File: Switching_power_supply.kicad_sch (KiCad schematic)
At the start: 20 parts, among them J10 Conn_01x02, J11 Conn_01x02, J12 Conn_01x02, J8 Conn_01x03_Pin, J9 Conn_01x02, U4 AMS1117, U5 LM2596HVS-ADJRG

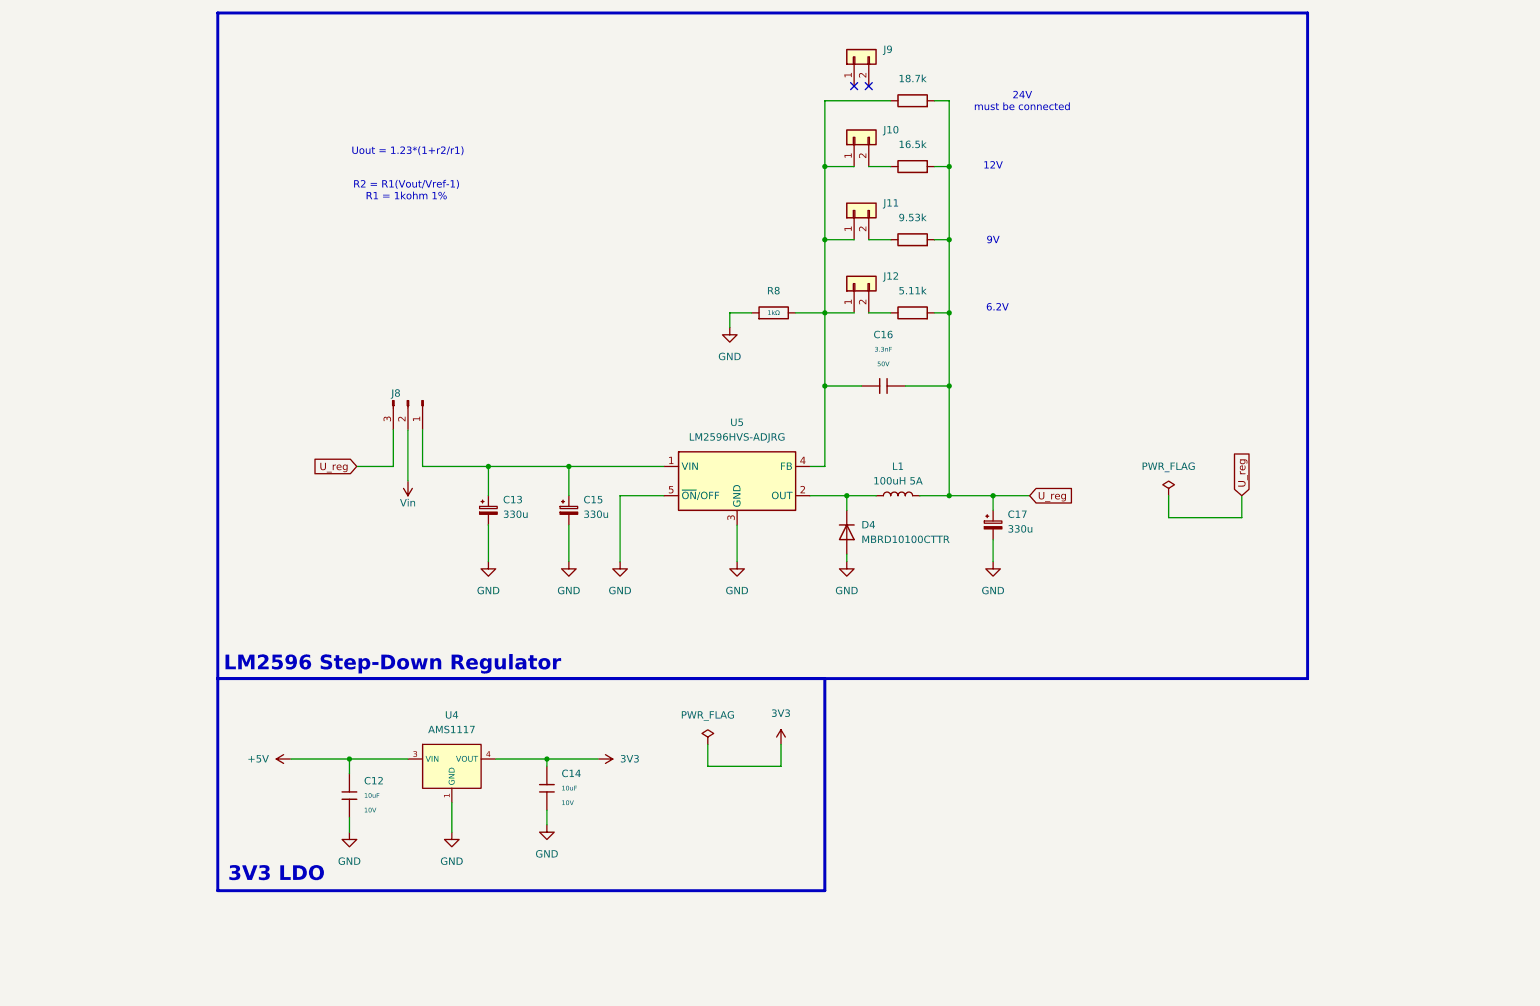
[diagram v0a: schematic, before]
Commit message: Added mechanical standard and updated readme
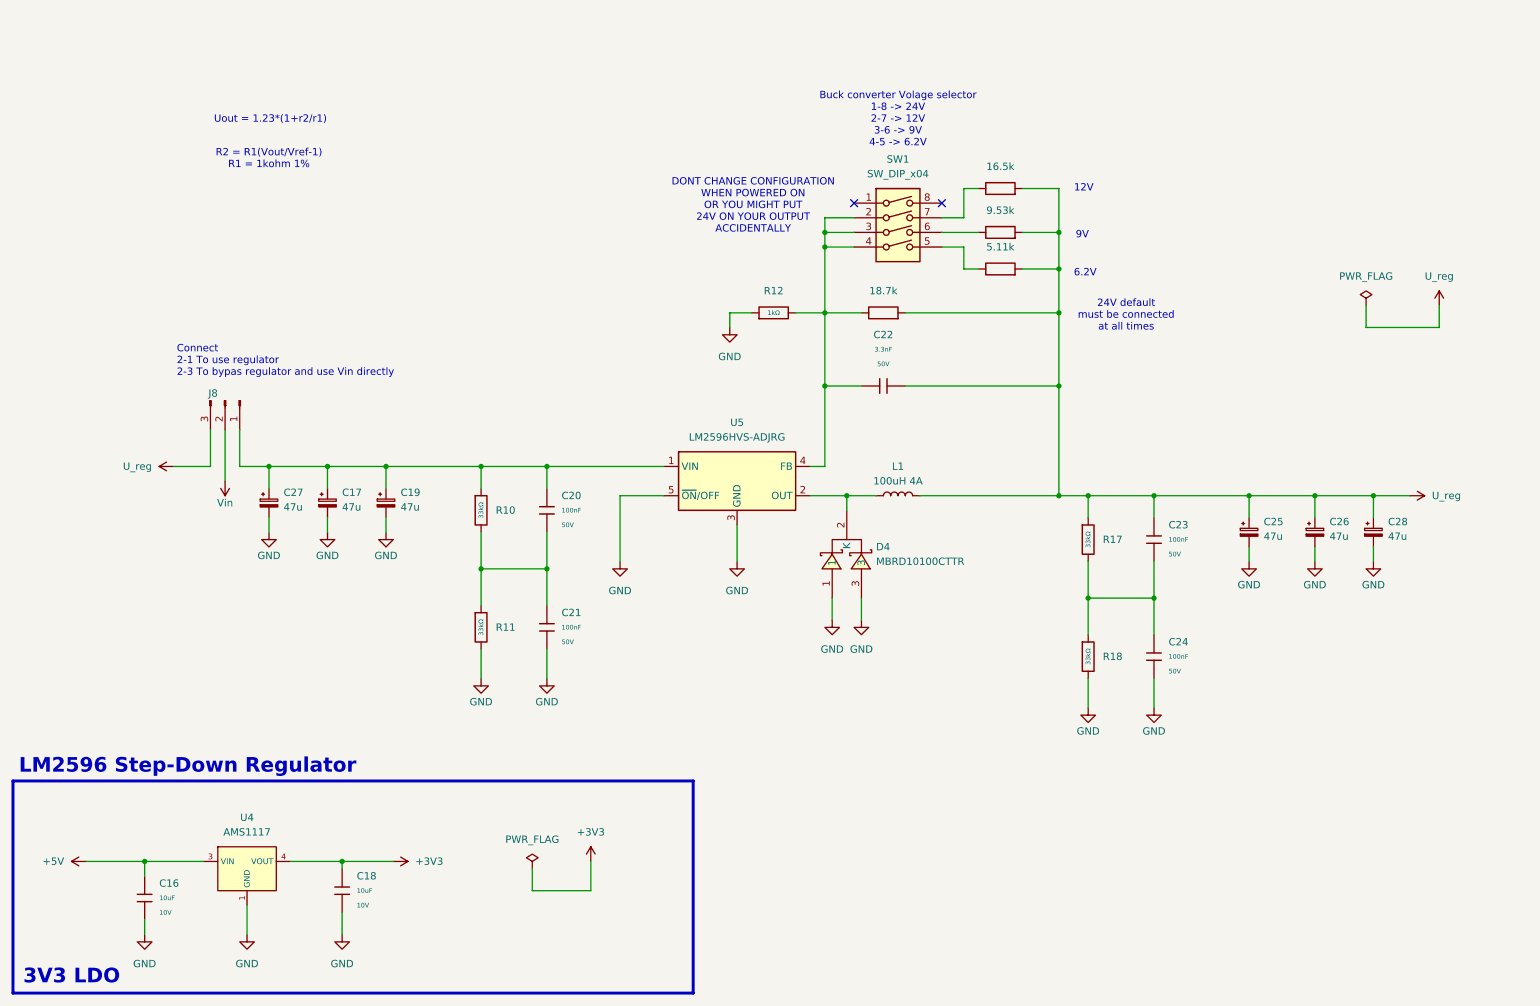
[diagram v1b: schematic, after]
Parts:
- removed C13, C15: 330u, symbol Device:C_Polarized_Small
- removed D4: MBRD10100CTTR, symbol Device:D
- removed J10, J11, J12, J9: Conn_01x02, symbol Connector_Generic:Conn_01x02
- added C19, C25, C26, C27, C28: 47u, Capacitor_SMD:CP_Elec_6.3x7.7, symbol Device:C_Polarized_Small
- added C20, C21, C23, C24: 100nF, PCM_JLCPCB:C_0603, symbol PCM_JLCPCB-Capacitors:0603,100nF
- added D4: MBRD10100CTTR, SMC_MBRD10100CTTR:TO-252-3_L6.5-W5.8-P4.58-TL, symbol SMC_MBRD10100CTTR:MBRD10100CTTR
- added R10, R11, R17, R18: 33kΩ, PCM_JLCPCB:R_0402, symbol PCM_JLCPCB-Resistors:0402,33kΩ
- added SW1: SW_DIP_x04, Button_Switch_THT:SW_DIP_SPSTx04_Slide_6.7x11.72mm_W7.62mm_P2.54mm_LowProfile, symbol Switch:SW_DIP_x04
- C17: value 330u -> 47u; footprint (none) -> Capacitor_SMD:CP_Elec_6.3x7.7; LCSC C178734 -> C7461235
- J8: footprint (none) -> Connector_PinHeader_2.54mm:PinHeader_1x03_P2.54mm_Vertical
- L1: value 100uH 5A -> 100uH 4A; footprint (none) -> Inductor_SMD:L_Sunlord_SWRB1207S; LCSC C3007746 -> C5368704
- R13: renamed from R9; footprint (none) -> PCM_JLCPCB:R_0402; LCSC (none) -> C11476
- R14: renamed from R10; footprint (none) -> PCM_JLCPCB:R_0402; LCSC (none) -> C25857
- R15: renamed from R11; footprint (none) -> PCM_JLCPCB:R_0402; LCSC (none) -> C295883
- R16: renamed from R12; footprint (none) -> PCM_JLCPCB:R_0402; LCSC (none) -> C274895
- renumbered C12 to C16, C14 to C18, C16 to C22, R8 to R12
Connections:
- net GND: now also C19.2, C21.2, C24.2, C25.2, C26.2, C27.2, C28.2, D4.1, D4.3, R11.2, R18.2
- net U_reg: now also C23.1, C25.1, C26.1, C28.1, R17.1; no longer C17.1
- net at L1.1, U5.2 (OUT): now also D4.2 (K)
- net at C22.1, R12.2, R13.1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: now also SW1.2, SW1.3, SW1.4
- net at R16.1: now also SW1.5
- net at J8.1 (Pin_1), U5.1 (VIN): now also C17.1, C19.1, C20.1, C27.1, R10.1
- net at R15.1: now also SW1.6
- net at R14.1: now also SW1.7
- net 3V3 renamed +3V3
- new net: C20.2, C21.1, R10.2, R11.1
- new net: C23.2, C24.1, R17.2, R18.1
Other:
- note added: "24V default must be connected at all times"
- note added: "Buck converter Volage selector 1-8 -> 24V 2-7 -> 12V 3-6 -> 9V 4-5 -> 6.2V"
- note added: "Connect 2-1 To use regulator 2-3 To bypas regulator and use Vin directly"
- note added: "DONT CHANGE CONFIGURATION WHEN POWERED ON OR YOU MIGHT PUT 24V ON YOUR OUTPUT ACCIDENTALLY"
- note removed: "24V must be connected"
- moved on the sheet: C16, C18, J8, U4

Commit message: updated XT60 place. added routing
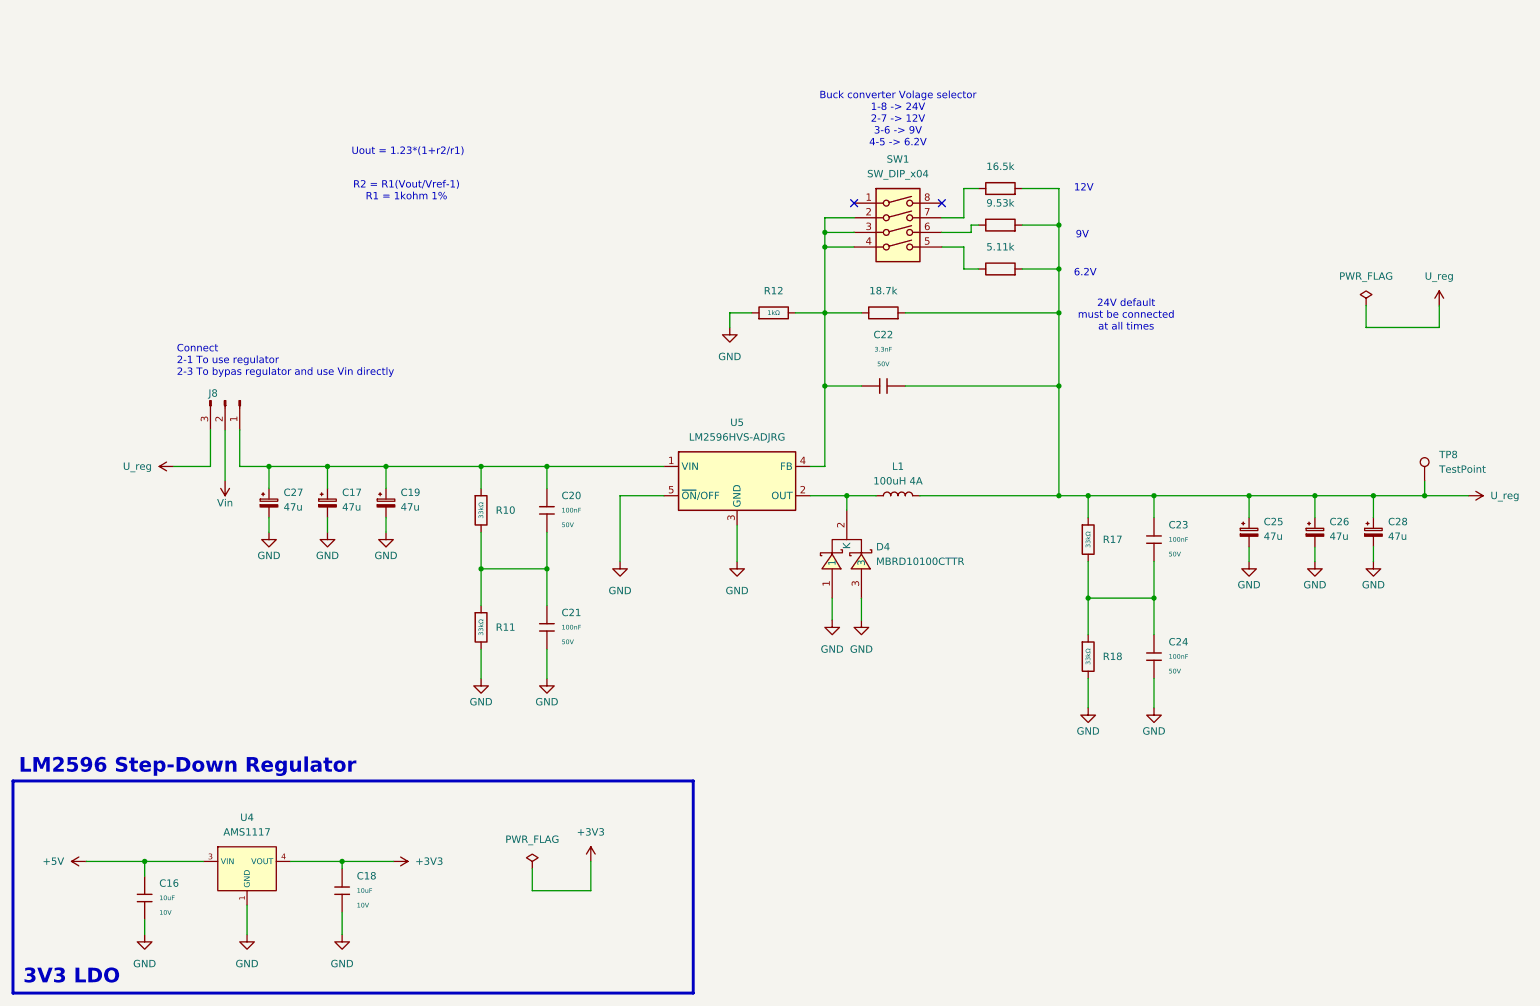
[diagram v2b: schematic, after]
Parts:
- added TP8: TestPoint, TestPoint:TestPoint_Pad_D1.0mm, symbol Connector:TestPoint
- L1: LCSC C5368704 -> C5368704
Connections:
- net U_reg: now also TP8.1
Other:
- note removed: "DONT CHANGE CONFIGURATION WHEN POWERED ON OR YOU MIGHT PUT 24V ON YOUR OUTPUT ACCIDENTALLY"
- title: (none) -> MMS3 Stepper Controler
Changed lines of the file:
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@@
 	(generator_version "9.0")
 	(paper "A4")
+	(title_block
+		(title "MMS3 Stepper Controler")
+		(date "2026-02-25")
+		(rev "R0")
+		(comment 1 "Made by Wojciech Szafrański")
+		(comment 2 "Designed in poland")
+		(comment 3 "MMS3 Hat based on Chainbus")
+	)
 	(rectangle
 		(start 13.97 161.29)
@@
 	(text "R2 = R1(Vout/Vref-1)\nR1 = 1kohm 1%\n"
 		(exclude_from_sim no)
-		(at 58.42 53.34 0)
+		(at 82.296 58.928 0)
 		(effects
 			(font
@@
 	(text "Uout = 1.23*(1+r2/r1)\n"
 		(exclude_from_sim no)
-		(at 58.674 46.482 0)
+		(at 82.55 52.07 0)
 		(effects
 			(font
@@
 		)
 	)
-	(text "DONT CHANGE CONFIGURATION\nWHEN POWERED ON\nOR YOU MIGHT PUT\n24V ON YOUR OUTPUT\nACCIDENTALLY"
-		(exclude_from_sim no)
-		(at 142.494 61.468 0)
-		(effects
-			(font
-				(size 1.27 1.27)
-				(color 255 0 0 1)
-			)
-		)
-	)
 	(text "24V default\nmust be connected\nat all times"
 		(exclude_from_sim no)
@@
 	)
 	(junction
-		(at 195.58 66.04)
+		(at 228.6 111.76)
 		(diameter 0)
 		(color 0 0 0 0)
 	)
 	(junction
-		(at 228.6 111.76)
+		(at 200.66 111.76)
 		(diameter 0)
 		(color 0 0 0 0)
 	)
 	(junction
-		(at 200.66 111.76)
+		(at 158.75 111.76)
 		(diameter 0)
 		(color 0 0 0 0)
 	)
 	(junction
-		(at 158.75 111.76)
+		(at 195.58 64.77)
 		(diameter 0)
 		(color 0 0 0 0)
@@
 	)
 	(junction
+		(at 259.08 111.76)
+		(diameter 0)
+		(color 0 0 0 0)
+	)
+	(junction
 		(at 106.68 124.46)
 		(diameter 0)
@@
 	(wire
 		(pts
+			(xy 259.08 111.76) (xy 266.7 111.76)
+		)
+		(stroke
+			(width 0)
+			(type default)
+		)
+	)
+	(wire
+		(pts
 			(xy 168.91 80.01) (xy 195.58 80.01)
 		)
@@
 	(wire
 		(pts
+			(xy 180.34 66.04) (xy 175.26 66.04)
+		)
+		(stroke
+			(width 0)
+			(type default)
+		)
+	)
+	(wire
+		(pts
 			(xy 212.09 123.19) (xy 212.09 129.54)
 		)
@@
 	(wire
 		(pts
-			(xy 195.58 66.04) (xy 195.58 72.39)
-		)
-		(stroke
-			(width 0)
-			(type default)
-		)
-	)
-	(wire
-		(pts
 			(xy 195.58 111.76) (xy 200.66 111.76)
 		)
@@
 	(wire
 		(pts
-			(xy 189.23 66.04) (xy 195.58 66.04)
+			(xy 189.23 64.77) (xy 195.58 64.77)
 		)
 		(stroke
@@
 	(wire
 		(pts
-			(xy 250.19 111.76) (xy 256.54 111.76)
+			(xy 250.19 111.76) (xy 259.08 111.76)
 		)
 		(stroke
@@
 	(wire
 		(pts
-			(xy 195.58 58.42) (xy 195.58 66.04)
+			(xy 195.58 58.42) (xy 195.58 64.77)
 		)
 		(stroke
@@
 	(wire
 		(pts
+			(xy 195.58 64.77) (xy 195.58 72.39)
+		)
+		(stroke
+			(width 0)
+			(type default)
+		)
+	)
+	(wire
+		(pts
 			(xy 114.3 175.26) (xy 114.3 180.34)
 		)
@@
 	(wire
 		(pts
-			(xy 175.26 66.04) (xy 181.61 66.04)
+			(xy 180.34 64.77) (xy 181.61 64.77)
 		)
 		(stroke
@@
 	(wire
 		(pts
+			(xy 259.08 109.22) (xy 259.08 111.76)
+		)
+		(stroke
+			(width 0)
+			(type default)
+		)
+	)
+	(wire
+		(pts
 			(xy 200.66 111.76) (xy 212.09 111.76)
 		)
@@
 	(wire
 		(pts
+			(xy 180.34 64.77) (xy 180.34 66.04)
+		)
+		(stroke
+			(width 0)
+			(type default)
+		)
+	)
+	(wire
+		(pts
 			(xy 200.66 129.54) (xy 200.66 135.89)
 		)
@@
 	)
 	(image
-		(at 88.9 49.53)
+		(at 112.776 55.118)
 		(scale 0.441642)
 		(data "iVBORw0KGgoAAAANSUhEUgAAAWQAAAD+CAYAAAANkX+xAAAAAXNSR0IArs4c6QAAAARnQU1BAACx"
@@
 	(symbol
 		(lib_id "power:+5V")
-		(at 256.54 111.76 270)
+		(at 266.7 111.76 270)
 		(mirror x)
 		(unit 1)
@@
 		(fields_autoplaced yes)
 		(property "Reference" "#PWR090"
-			(at 252.73 111.76 0)
+			(at 262.89 111.76 0)
 			(effects
 				(font
@@
 		)
 		(property "Value" "U_reg"
-			(at 260.35 111.7599 90)
+			(at 270.51 111.7599 90)
 			(effects
 				(font
@@
 		)
 		(property "Footprint" ""
-			(at 256.54 111.76 0)
+			(at 266.7 111.76 0)
 			(effects
 				(font
@@
 		)
 		(property "Datasheet" ""
-			(at 256.54 111.76 0)
+			(at 266.7 111.76 0)
 			(effects
 				(font
@@
 		)
 		(property "Description" "Power symbol creates a global label with name \"+5V\""
-			(at 256.54 111.76 0)
+			(at 266.7 111.76 0)
 			(effects
 				(font
@@
 	)
 	(symbol
+		(lib_id "Connector:TestPoint")
+		(at 259.08 109.22 0)
+		(unit 1)
+		(exclude_from_sim no)
+		(in_bom yes)
+		(on_board yes)
+		(dnp no)
+		(fields_autoplaced yes)
+		(property "Reference" "TP8"
+			(at 261.62 104.6479 0)
+			(effects
+				(font
+					(size 1.27 1.27)
+				)
+				(justify left)
+			)
+		)
+		(property "Value" "TestPoint"
+			(at 261.62 107.1879 0)
+			(effects
+				(font
+					(size 1.27 1.27)
+				)
+				(justify left)
+			)
+		)
+		(property "Footprint" "TestPoint:TestPoint_Pad_D1.0mm"
+			(at 264.16 109.22 0)
+			(effects
+				(font
+					(size 1.27 1.27)
+				)
+				(hide yes)
+			)
+		)
+		(property "Datasheet" "~"
+			(at 264.16 109.22 0)
+			(effects
+				(font
+					(size 1.27 1.27)
+				)
+				(hide yes)
+			)
+		)
+		(property "Description" "test point"
+			(at 259.08 109.22 0)
+			(effects
+				(font
+					(size 1.27 1.27)
+				)
+				(hide yes)
+			)
+		)
+		(pin "1"
+		)
+		(instances
+			(project "MMS3_hat_stepper_controler"
+				(path "/6596548a-44e0-46d8-8624-fd71cf4a3e17/c6fe6645-c1eb-4317-9e6f-134a73c9fa05"
+					(reference "TP8")
+					(unit 1)
+				)
+			)
+		)
+	)
+	(symbol
 		(lib_id "Connector:Conn_01x03_Pin")
 		(at 50.8 95.25 270)
@@
 			)
 		)
-		(property "LCSC" " C5368704"
+		(property "LCSC" "C5368704"
 			(at 167.64 111.76 90)
 			(effects
@@
 	(symbol
 		(lib_id "Device:R")
-		(at 185.42 66.04 90)
+		(at 185.42 64.77 90)
 		(unit 1)
 		(exclude_from_sim no)
@@
 		(fields_autoplaced yes)
 		(property "Reference" "R15"
-			(at 185.42 59.69 90)
+			(at 185.42 58.42 90)
 			(effects
 				(font
@@
 		)
 		(property "Value" "9.53k"
-			(at 185.42 62.23 90)
+			(at 185.42 60.96 90)
 			(effects
 				(font
@@
 		)
 		(property "Footprint" "PCM_JLCPCB:R_0402"
-			(at 185.42 67.818 90)
+			(at 185.42 66.548 90)
 			(effects
 				(font
@@
 		)
 		(property "Datasheet" "~"
-			(at 185.42 66.04 0)
+			(at 185.42 64.77 0)
 			(effects
 				(font
@@
 		)
 		(property "Description" "Resistor"
-			(at 185.42 66.04 0)
+			(at 185.42 64.77 0)
 			(effects
 				(font
@@
 		)
 		(property "LCSC" "C295883"
-			(at 185.42 66.04 90)
+			(at 185.42 64.77 90)
 			(effects
 				(font
@@
 		)
 		(property "Sim.Device" ""
-			(at 185.42 66.04 90)
+			(at 185.42 64.77 90)
 			(effects
 				(font
@@
 		)
 		(instances
-			(project "MMS2_hat_template_small"
+			(project "MMS3_hat_stepper_controler"
 				(path "/6596548a-44e0-46d8-8624-fd71cf4a3e17/c6fe6645-c1eb-4317-9e6f-134a73c9fa05"
 					(reference "R15")

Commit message: moved I2C header to the side
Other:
- title: MMS3 Stepper Controler -> MMS3 Hat template small (Change Me)
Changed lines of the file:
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@@
 	(paper "A4")
 	(title_block
-		(title "MMS3 Stepper Controler")
+		(title "MMS3 Hat template small (Change Me)")
 		(date "2026-02-25")
-		(rev "R0")
+		(rev "A")
 		(comment 1 "Made by Wojciech Szafrański")
 		(comment 2 "Designed in poland")
-		(comment 3 "MMS3 Hat based on Chainbus")
 	)
 	(rectangle
